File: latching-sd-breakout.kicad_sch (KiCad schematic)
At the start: 6 parts, among them X1 microSD

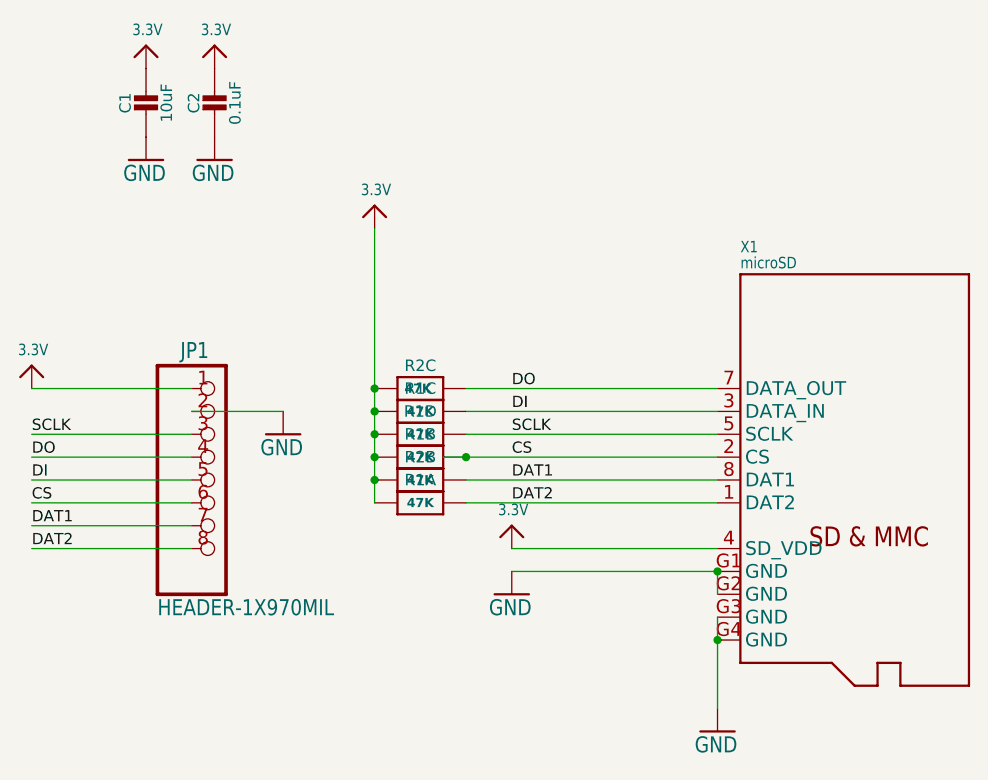
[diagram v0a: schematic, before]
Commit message: fix routing angles
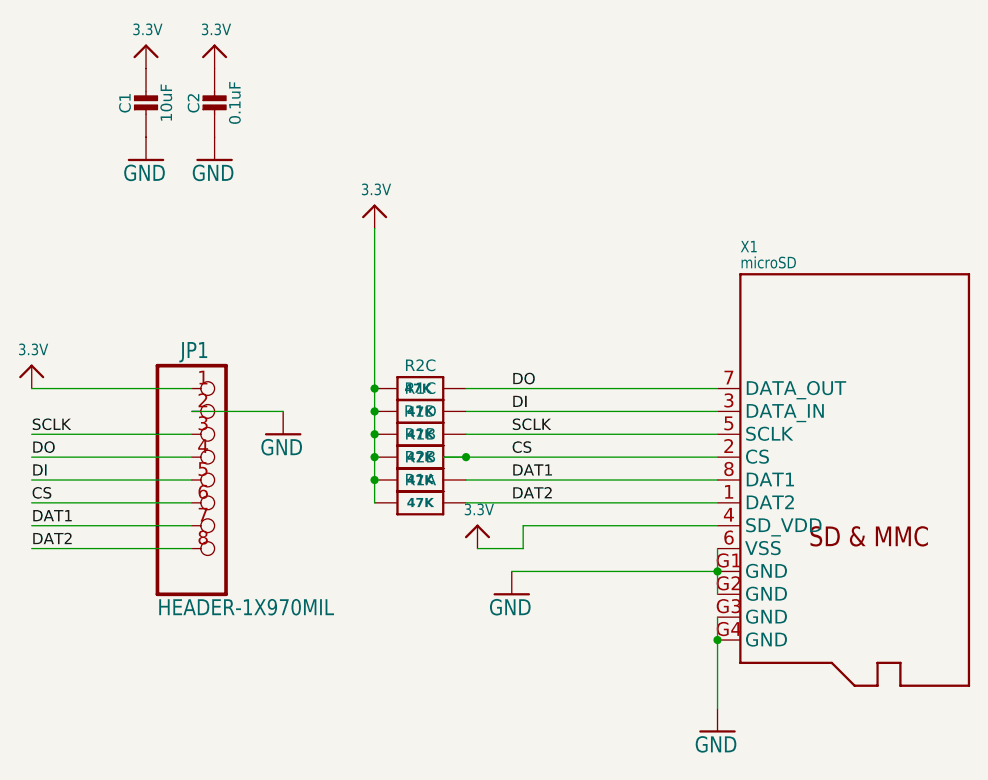
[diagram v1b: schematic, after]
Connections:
- net GND: now also X1.6 (VSS)
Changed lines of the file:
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@@
+	(wire
+		(pts
+			(xy 163.83 119.38) (xy 163.83 121.92)
+		)
+		(stroke
+			(width 0)
+			(type default)
+		)
+	)
+	(wire
+		(pts
+			(xy 142.24 116.84) (xy 163.83 116.84)
+		)
+		(stroke
+			(width 0.1524)
+			(type solid)
+		)
+	)
 	(wire
 		(pts
@@
 	(wire
 		(pts
+			(xy 142.24 119.38) (xy 142.24 116.84)
+		)
+		(stroke
+			(width 0.1524)
+			(type solid)
+		)
+	)
+	(wire
+		(pts
 			(xy 125.73 104.14) (xy 125.73 101.6)
 		)
@@
 	(wire
 		(pts
-			(xy 163.83 119.38) (xy 140.97 119.38)
+			(xy 142.24 119.38) (xy 137.16 119.38)
 		)
 		(stroke
@@
 		(pin "G4"
 		)
+		(pin "6"
+		)
 		(instances
 			(project ""
@@
 	(symbol
 		(lib_id "poop-eagle-import:3.3V")
-		(at 140.97 116.84 0)
+		(at 137.16 116.84 0)
 		(unit 1)
 		(exclude_from_sim no)
@@
 		(dnp no)
 		(property "Reference" "#U$5"
-			(at 140.97 116.84 0)
+			(at 137.16 116.84 0)
 			(effects
 				(font
@@
 		)
 		(property "Value" "3.3V"
-			(at 139.446 115.824 0)
+			(at 135.636 115.824 0)
 			(effects
 				(font
@@
 		)
 		(property "Footprint" ""
-			(at 140.97 116.84 0)
-			(effects
-				(font
-					(size 1.27 1.27)
-				)
-				(hide yes)
-			)
-		)
-		(property "Datasheet" ""
-			(at 140.97 116.84 0)
-			(effects
-				(font
-					(size 1.27 1.27)
-				)
-				(hide yes)
-			)
-		)
-		(property "Description" ""
-			(at 140.97 116.84 0)
-			(effects
-				(font
+			(at 137.16 116.84 0)
+			(effects
+				(font
+					(size 1.27 1.27)
+				)
+				(hide yes)
+			)
+		)
+		(property "Datasheet" ""
+			(at 137.16 116.84 0)
+			(effects
+				(font
+					(size 1.27 1.27)
+				)
+				(hide yes)
+			)
+		)
+		(property "Description" ""
+			(at 137.16 116.84 0)
+			(effects
+				(font

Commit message: changed resistor arrays
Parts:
- R1, R2: footprint Resistor_SMD:R_Array_Convex_4x0603 -> Resistor_SMD:R_Array_Convex_4x0502
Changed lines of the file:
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@@
 			)
 		)
-		(property "Footprint" "Resistor_SMD:R_Array_Convex_4x0603"
+		(property "Footprint" "Resistor_SMD:R_Array_Convex_4x0502"
 			(at 130.81 106.68 0)
 			(effects
@@
 			)
 		)
-		(property "Footprint" "Resistor_SMD:R_Array_Convex_4x0603"
+		(property "Footprint" "Resistor_SMD:R_Array_Convex_4x0502"
 			(at 130.81 109.22 0)
 			(effects
@@
 			)
 		)
-		(property "Footprint" "Resistor_SMD:R_Array_Convex_4x0603"
+		(property "Footprint" "Resistor_SMD:R_Array_Convex_4x0502"
 			(at 130.81 104.14 0)
 			(effects
@@
 			)
 		)
-		(property "Footprint" "Resistor_SMD:R_Array_Convex_4x0603"
+		(property "Footprint" "Resistor_SMD:R_Array_Convex_4x0502"
 			(at 130.81 101.6 0)
 			(effects
@@
 			)
 		)
-		(property "Footprint" "Resistor_SMD:R_Array_Convex_4x0603"
+		(property "Footprint" "Resistor_SMD:R_Array_Convex_4x0502"
 			(at 130.81 114.3 0)
 			(effects
@@
 			)
 		)
-		(property "Footprint" "Resistor_SMD:R_Array_Convex_4x0603"
+		(property "Footprint" "Resistor_SMD:R_Array_Convex_4x0502"
 			(at 130.81 111.76 0)
 			(effects

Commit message: replace 0502 resister arrays with 0603
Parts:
- R1, R2: footprint Resistor_SMD:R_Array_Convex_4x0502 -> Resistor_SMD:R_Array_Concave_4x0603
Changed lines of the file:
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@@
 			)
 		)
-		(property "Footprint" "Resistor_SMD:R_Array_Convex_4x0502"
+		(property "Footprint" "Resistor_SMD:R_Array_Concave_4x0603"
 			(at 130.81 106.68 0)
 			(effects
@@
 			)
 		)
-		(property "Footprint" "Resistor_SMD:R_Array_Convex_4x0502"
+		(property "Footprint" "Resistor_SMD:R_Array_Concave_4x0603"
 			(at 130.81 109.22 0)
 			(effects
@@
 			)
 		)
-		(property "Footprint" "Resistor_SMD:R_Array_Convex_4x0502"
+		(property "Footprint" "Resistor_SMD:R_Array_Concave_4x0603"
 			(at 130.81 104.14 0)
 			(effects
@@
 			)
 		)
-		(property "Footprint" "Resistor_SMD:R_Array_Convex_4x0502"
+		(property "Footprint" "Resistor_SMD:R_Array_Concave_4x0603"
 			(at 130.81 101.6 0)
 			(effects
@@
 			)
 		)
-		(property "Footprint" "Resistor_SMD:R_Array_Convex_4x0502"
+		(property "Footprint" "Resistor_SMD:R_Array_Concave_4x0603"
 			(at 130.81 114.3 0)
 			(effects
@@
 			)
 		)
-		(property "Footprint" "Resistor_SMD:R_Array_Convex_4x0502"
+		(property "Footprint" "Resistor_SMD:R_Array_Concave_4x0603"
 			(at 130.81 111.76 0)
 			(effects
